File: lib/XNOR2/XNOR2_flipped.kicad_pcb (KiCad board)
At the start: 2 copper layers, 10 parts, among them P1 PMOS, P2 PMOS, P3 PMOS, P4 PMOS, P5 PMOS

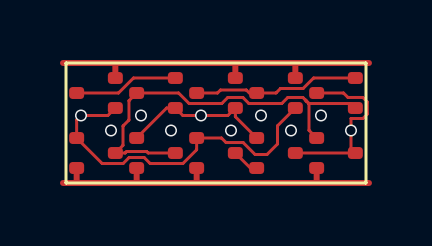
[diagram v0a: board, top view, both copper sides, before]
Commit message: Layout of XOR2 and XNOR2, in both orientations. That nut was hard to crack !!
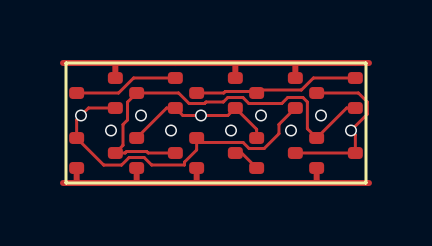
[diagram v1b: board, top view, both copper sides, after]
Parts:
- moved N3 2.83 mm to (7.00, 1.00), turned to 180 degrees
- moved N4 2.83 mm to (5.00, 1.00), turned to 180 degrees
- moved P3 2.83 mm to (5.00, 3.00), turned to 0 degrees
- moved P4 2.83 mm to (7.00, 3.00), turned to 0 degrees
- moved N1 2.00 mm to (1.00, 1.00), turned to 180 degrees
- moved N2 2.00 mm to (3.00, 1.00), turned to 180 degrees
- moved N5 2.00 mm to (9.00, 1.00), turned to 180 degrees
- moved P1 2.00 mm to (1.00, 3.00), turned to 0 degrees
- moved P2 2.00 mm to (3.00, 3.00), turned to 0 degrees
- moved P5 2.00 mm to (9.00, 3.00), turned to 0 degrees
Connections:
- N1 pad 3: inor -> sndNA
- N2 pad 2: GND -> sndNA
- N2 pad 3: inor -> inand
- N3 pad 3: sndNA -> nmid
- N4 pad 2: sndNA -> GND
- N4 pad 3: Y -> nmid
- N5 pad 1: inor -> inand
- N5 pad 2: GND -> nmid
- P1 pad 3: sndPA -> inand
- P2 pad 2: sndPA -> VDD
- P2 pad 3: inor -> inand
- P3 pad 3: pmid -> sndPA
- P4 pad 2: VDD -> sndPA
- P4 pad 3: pmid -> Y
- P5 pad 1: inor -> inand
- P5 pad 2: pmid -> VDD
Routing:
- net inor: track 13.8 -> 0.00 mm
- net inand: track 0.00 -> 13.5 mm
- net pmid: track 5.58 -> 0.00 mm
- net nmid: track 0.00 -> 5.54 mm
- net sndNA: track 0.92 -> 3.50 mm
- net sndPA: track 3.50 -> 0.92 mm
- net GND: track 12.3 -> 11.7 mm
- net VDD: track 11.7 -> 12.2 mm
